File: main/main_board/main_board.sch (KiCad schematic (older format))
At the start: 0 parts

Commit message: Work on main board.
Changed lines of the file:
@@
 $Descr A4 11693 8268
 encoding utf-8
-Sheet 1 5
+Sheet 1 13
 Title ""
 Date ""
@@
 Text Notes 7200 6950 0    50   ~ 0
 The main board is system integration for the ILEMT tracker.\nIt connects the MicroZED SOC with the input boards and\nclock, and provides support for in the analog side \n(voltage reference and BIST).
+$Sheet
+S 2800 1850 1100 450
+U 5EC15224
+F0 "output_slot" 50
+F1 "output_slot.sch" 50
+$EndSheet
+$Sheet
+S 2800 2650 1100 450
+U 5EC4BDFA
+F0 "BIST_DAC" 50
+F1 "BIST.sch" 50
+$EndSheet
+$Sheet
+S 2950 4500 1100 450
+U 5E9C9ED4
+F0 "sheet5E9C9ED2" 50
+F1 "../../input/power.sch" 50
+$EndSheet
 $EndSCHEMATC

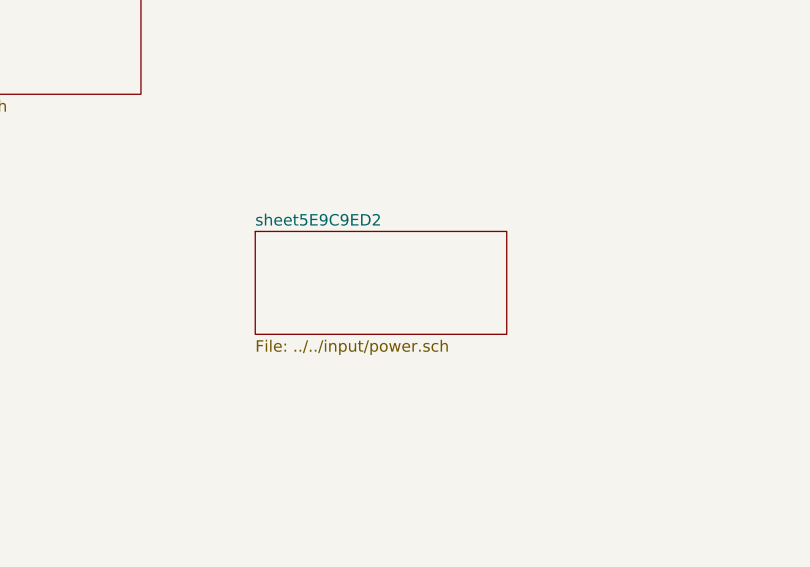
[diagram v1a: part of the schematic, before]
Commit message: Add lowpass filter to input board reference buffer, and fix antialias frequency response. Supply and reference testing in notebook.txt, lots of discussion of reference noise.
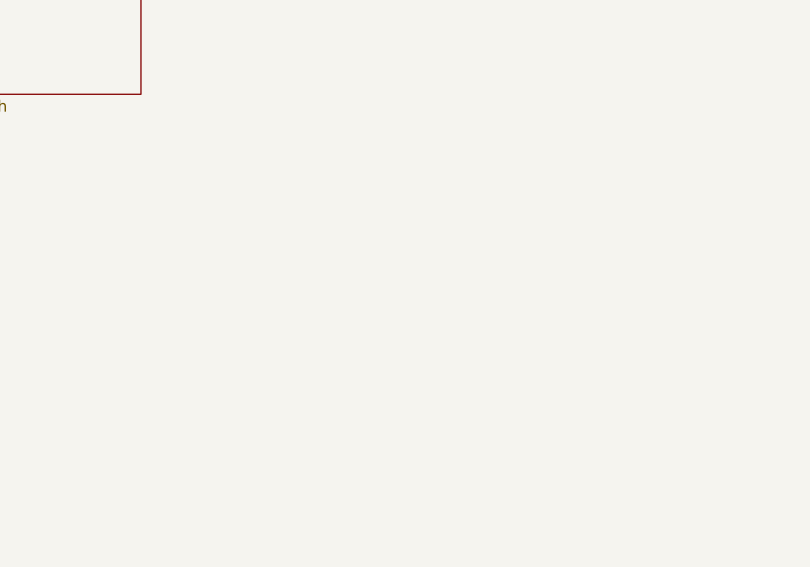
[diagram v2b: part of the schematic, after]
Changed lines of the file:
@@
 $Descr A4 11693 8268
 encoding utf-8
-Sheet 1 13
+Sheet 1 12
 Title ""
 Date ""
@@
 F1 "BIST.sch" 50
 $EndSheet
-$Sheet
-S 2950 4500 1100 450
-U 5E9C9ED4
-F0 "sheet5E9C9ED2" 50
-F1 "../../input/power.sch" 50
-$EndSheet
 $EndSCHEMATC

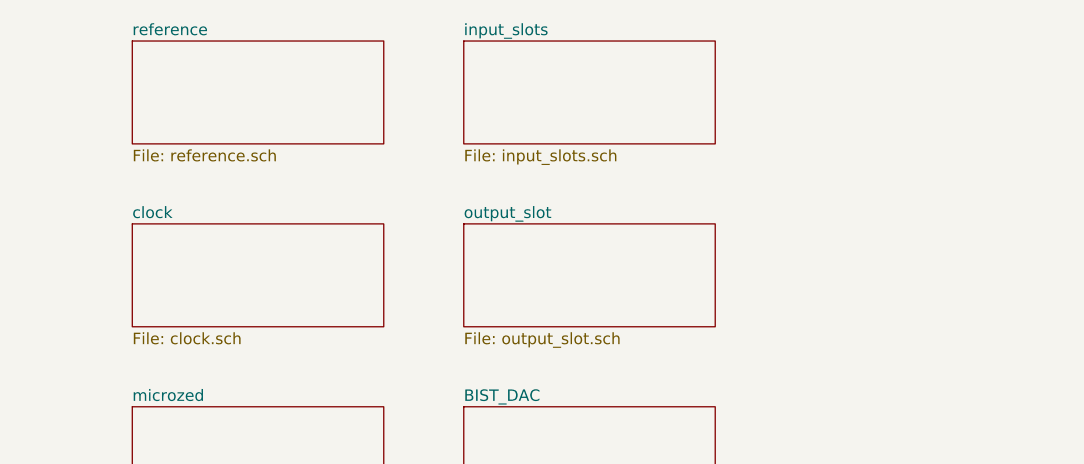
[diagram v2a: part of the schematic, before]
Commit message: A bunch of thinking about RFI and ESD, and some testing.  Mostly reflected in notebook.txt. Also another more explicit round of consideration of box-level grounding and power distribution, because this affects the power conditioning on the main board.  Power nets on the main board are mostly captured.  I added supply decoupling at each plugin slot.
in_filter.sxsch: added simulation of ESD, use vendor models for TVS diode and ferrite.

power_budget.xlsx: get rid of sheets for the input boards not implemented.  Add sheet for
the main board and carry over data from the input board sheet.
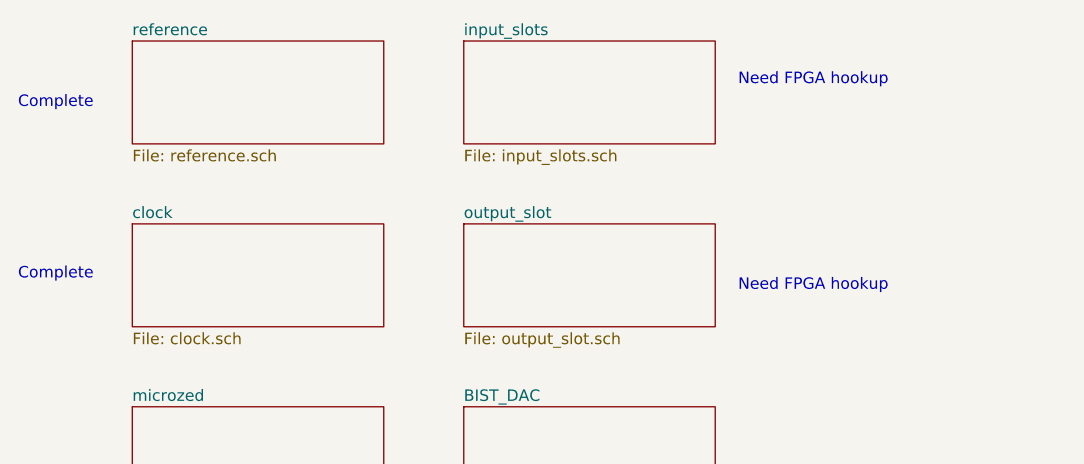
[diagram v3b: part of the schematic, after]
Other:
- note added: "Complete"
- note added: "Need FPGA hookup"
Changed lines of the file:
@@
 F1 "BIST.sch" 50
 $EndSheet
+Text Notes 850  2100 0    50   ~ 0
+Complete
+Text Notes 4000 1250 0    50   ~ 0
+Need FPGA hookup
+Text Notes 4000 2150 0    50   ~ 0
+Need FPGA hookup
+Text Notes 850  1350 0    50   ~ 0
+Complete
 $EndSCHEMATC

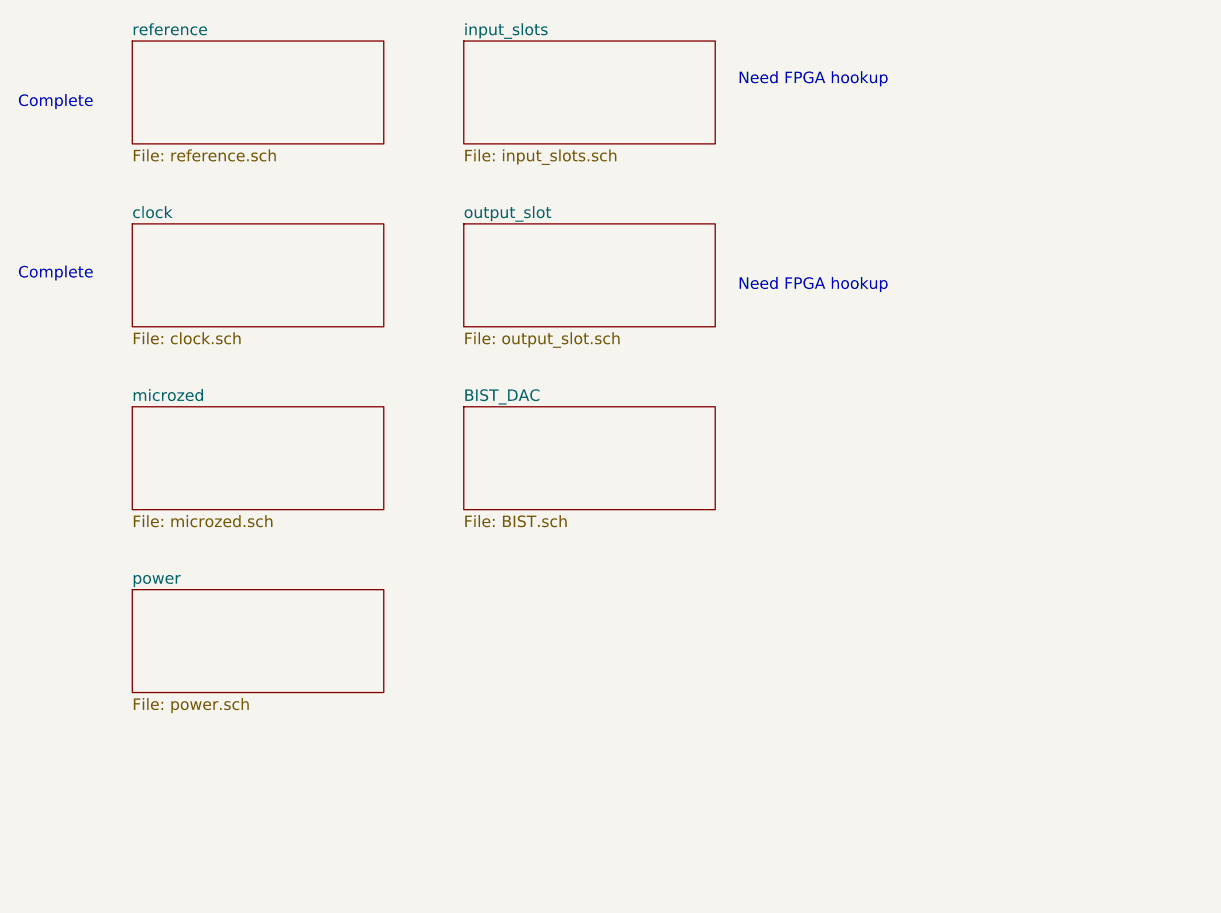
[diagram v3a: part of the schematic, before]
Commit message: Mostly work on hooking in the Microzed using kipart symbols and a footprint. Also added 2.5V VCCIO regulator.
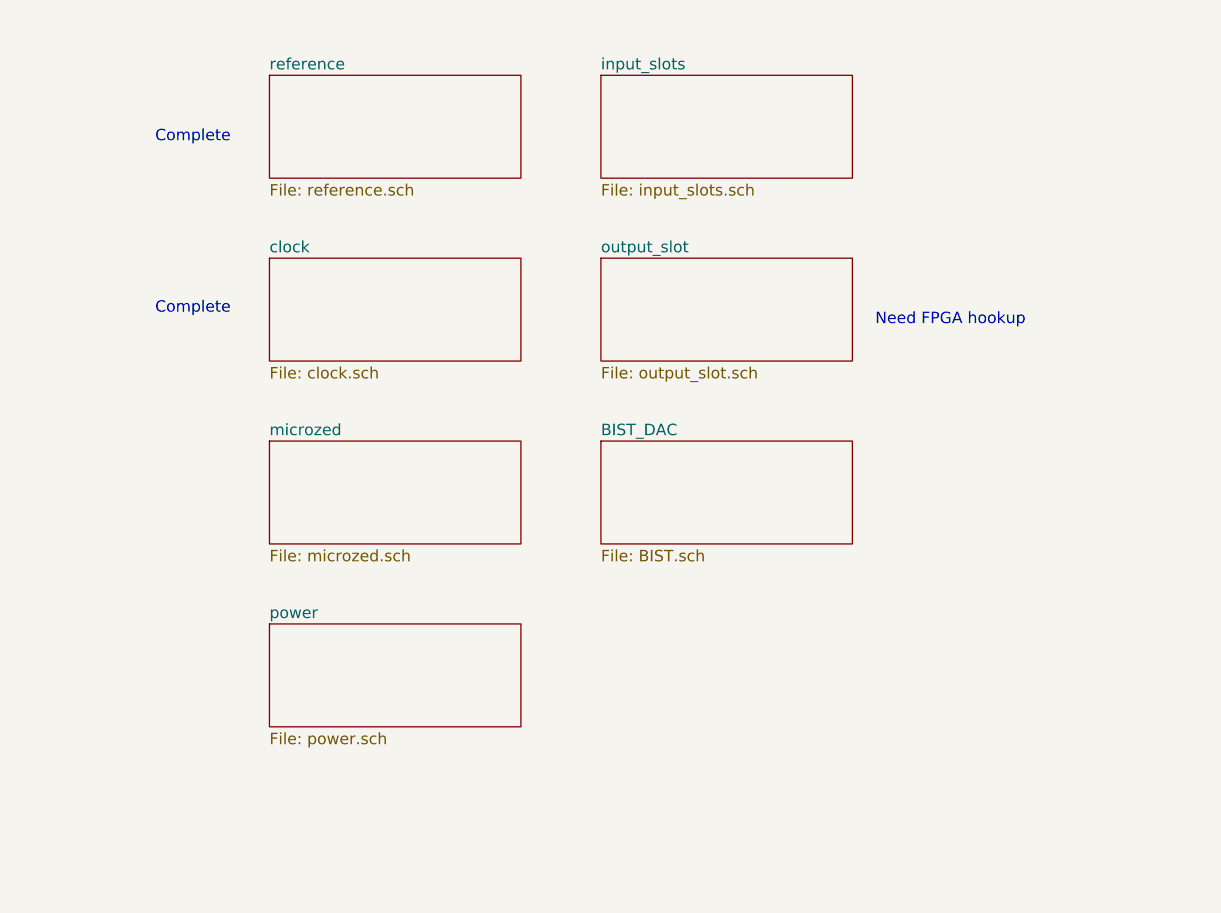
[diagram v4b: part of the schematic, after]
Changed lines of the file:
@@
 $EndDescr
 $Sheet
-S 1350 1050 1100 450
+S 1950 1200 1100 450
 U 5E525EB8
 F0 "reference" 50
@@
 $EndSheet
 $Sheet
-S 1350 1850 1100 450
+S 1950 2000 1100 450
 U 5E525F2C
 F0 "clock" 50
@@
 $EndSheet
 $Sheet
-S 1350 2650 1100 450
+S 1950 2800 1100 450
 U 5E525F87
 F0 "microzed" 50
@@
 $EndSheet
 $Sheet
-S 1350 3450 1100 450
+S 1950 3600 1100 450
 U 5E525FC9
 F0 "power" 50
@@
 $EndSheet
 $Sheet
-S 2800 1050 1100 450
+S 3400 1200 1100 450
 U 5E525FFE
 F0 "input_slots" 50
@@
 The main board is system integration for the ILEMT tracker.\nIt connects the MicroZED SOC with the input boards and\nclock, and provides support for in the analog side \n(voltage reference and BIST).
 $Sheet
-S 2800 1850 1100 450
+S 3400 2000 1100 450
 U 5EC15224
 F0 "output_slot" 50
@@
 $EndSheet
 $Sheet
-S 2800 2650 1100 450
+S 3400 2800 1100 450
 U 5EC4BDFA
 F0 "BIST_DAC" 50
 F1 "BIST.sch" 50
 $EndSheet
-Text Notes 850  2100 0    50   ~ 0
+Text Notes 1450 2250 0    50   ~ 0
 Complete
-Text Notes 4000 1250 0    50   ~ 0
+Text Notes 4600 2300 0    50   ~ 0
 Need FPGA hookup
-Text Notes 4000 2150 0    50   ~ 0
-Need FPGA hookup
-Text Notes 850  1350 0    50   ~ 0
+Text Notes 1450 1500 0    50   ~ 0
 Complete
 $EndSCHEMATC

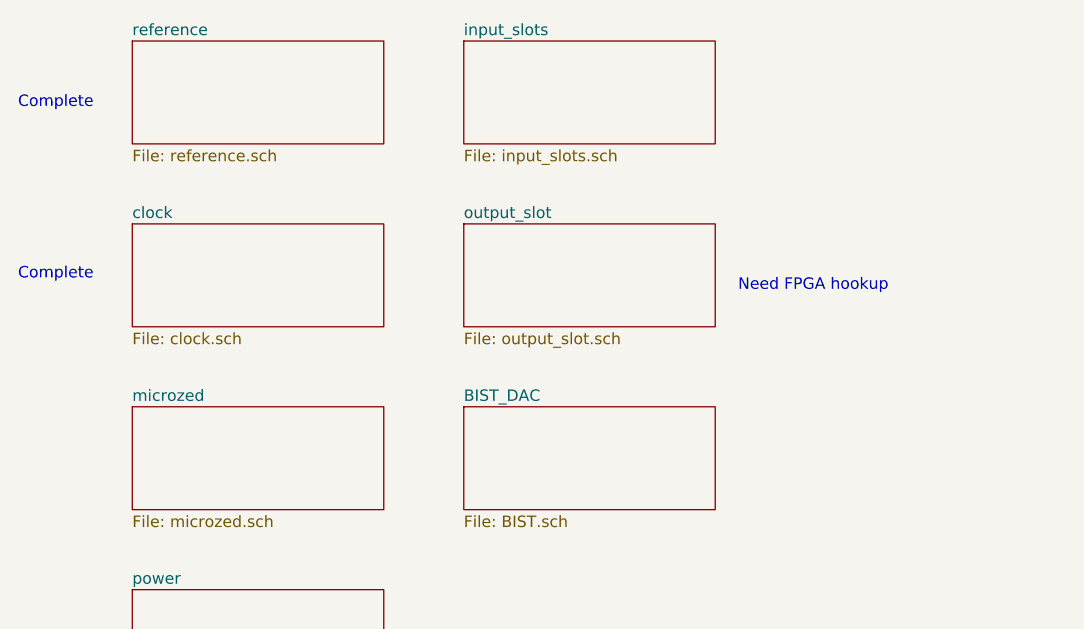
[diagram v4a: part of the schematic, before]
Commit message: Updated for new microzed pin mapping scheme.
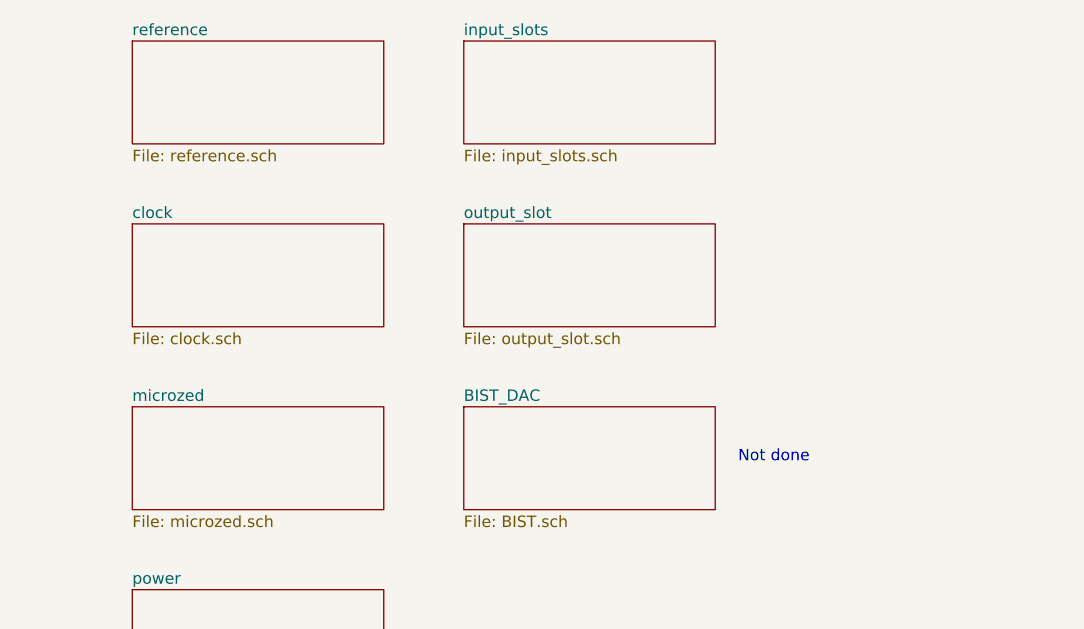
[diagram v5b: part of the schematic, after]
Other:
- note added: "Not done"
- note removed: "Complete"
- note removed: "Need FPGA hookup"
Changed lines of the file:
@@
 F1 "BIST.sch" 50
 $EndSheet
-Text Notes 1450 2250 0    50   ~ 0
-Complete
-Text Notes 4600 2300 0    50   ~ 0
-Need FPGA hookup
-Text Notes 1450 1500 0    50   ~ 0
-Complete
+Text Notes 4600 3050 0    50   ~ 0
+Not done
 $EndSCHEMATC

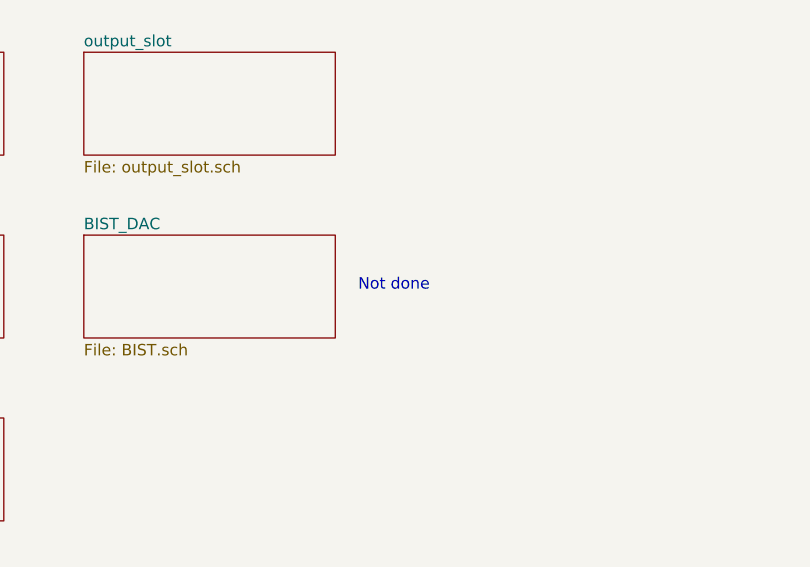
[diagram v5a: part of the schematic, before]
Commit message: Changes related to pin mapping. There's a new BIST unit in the Microzed symbol, and the unit ordering has changed. I also added SDI lines to the input slots which could be used to configure the ADC in a future version of the input board. Added some wire labels for easier routing.
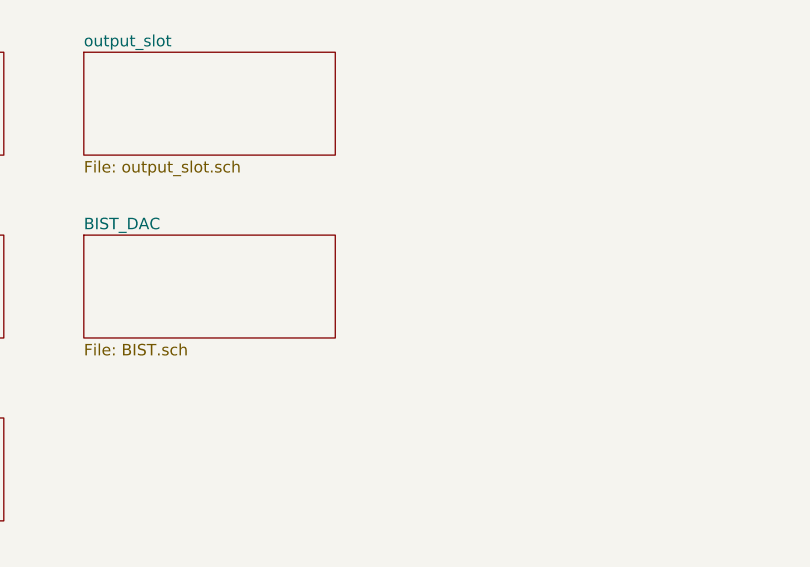
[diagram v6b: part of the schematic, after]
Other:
- note removed: "Not done"
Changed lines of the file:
@@
 F1 "BIST.sch" 50
 $EndSheet
-Text Notes 4600 3050 0    50   ~ 0
-Not done
 $EndSCHEMATC
